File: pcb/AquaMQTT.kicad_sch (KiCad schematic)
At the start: 22 parts, among them J1 DHW MAIN, J2 DHW HMI, J3 LLC 5V, J4 LLC 3V3, J5 Serial, J6 RTC DS3231, J7 Passthrough, Q1 BC547, Q2 BC547, Q3 BC547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

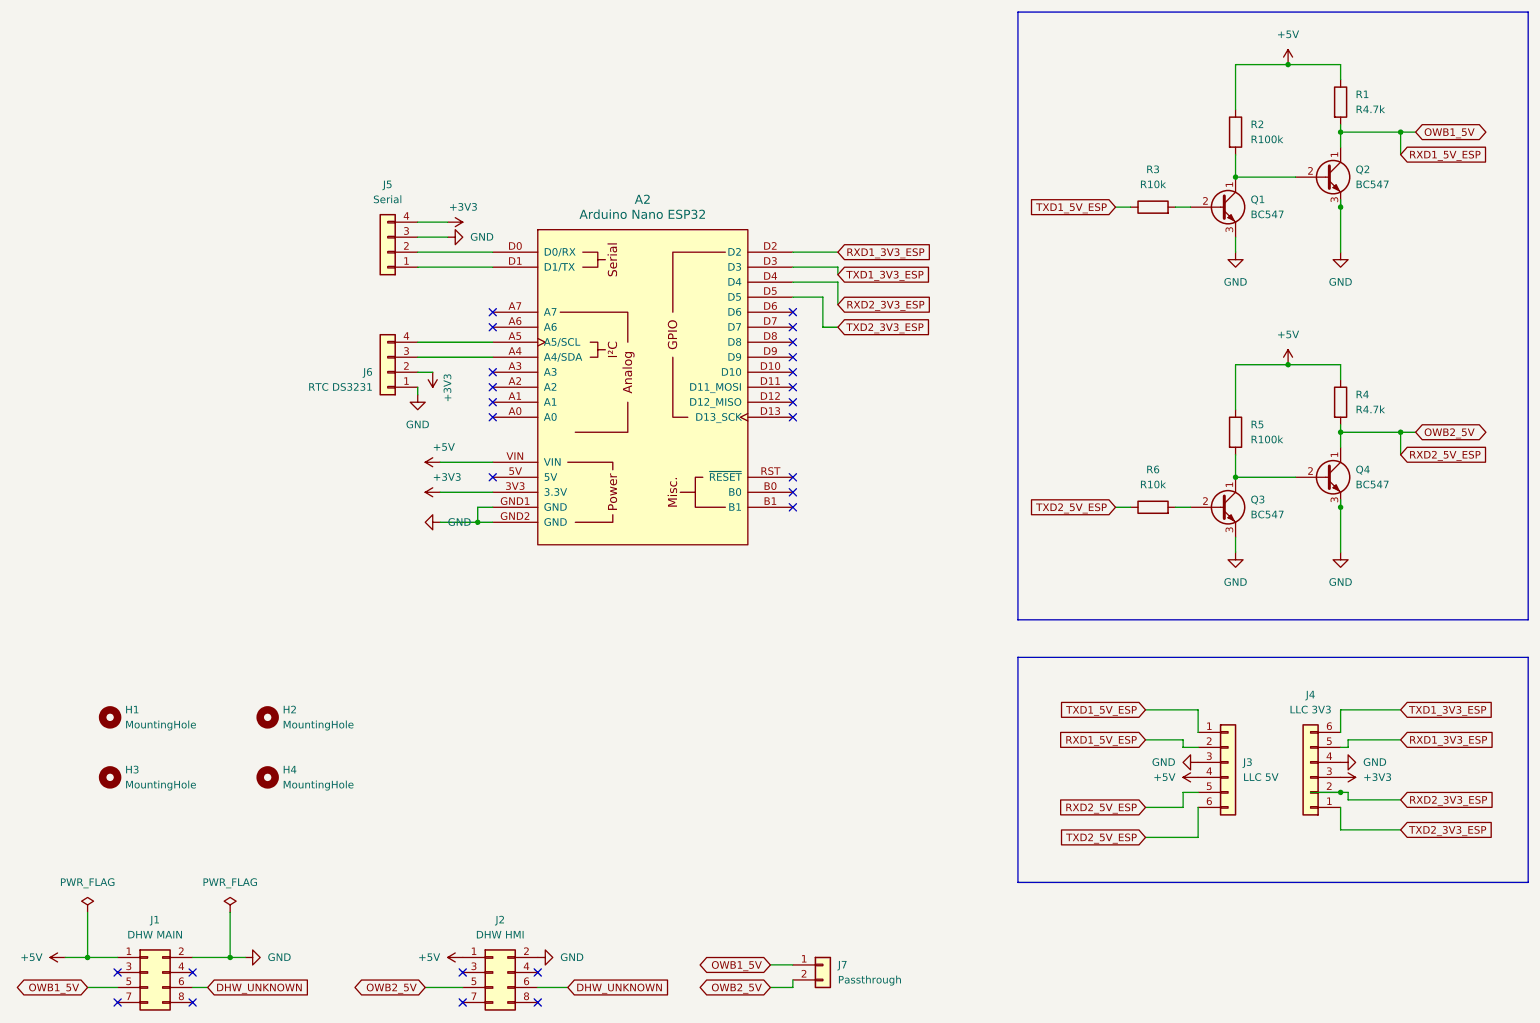
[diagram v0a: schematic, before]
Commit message: feat(pcb): added pcb in rev 2.0 (rast, pre-assembly, sn74lvct45) (#72)
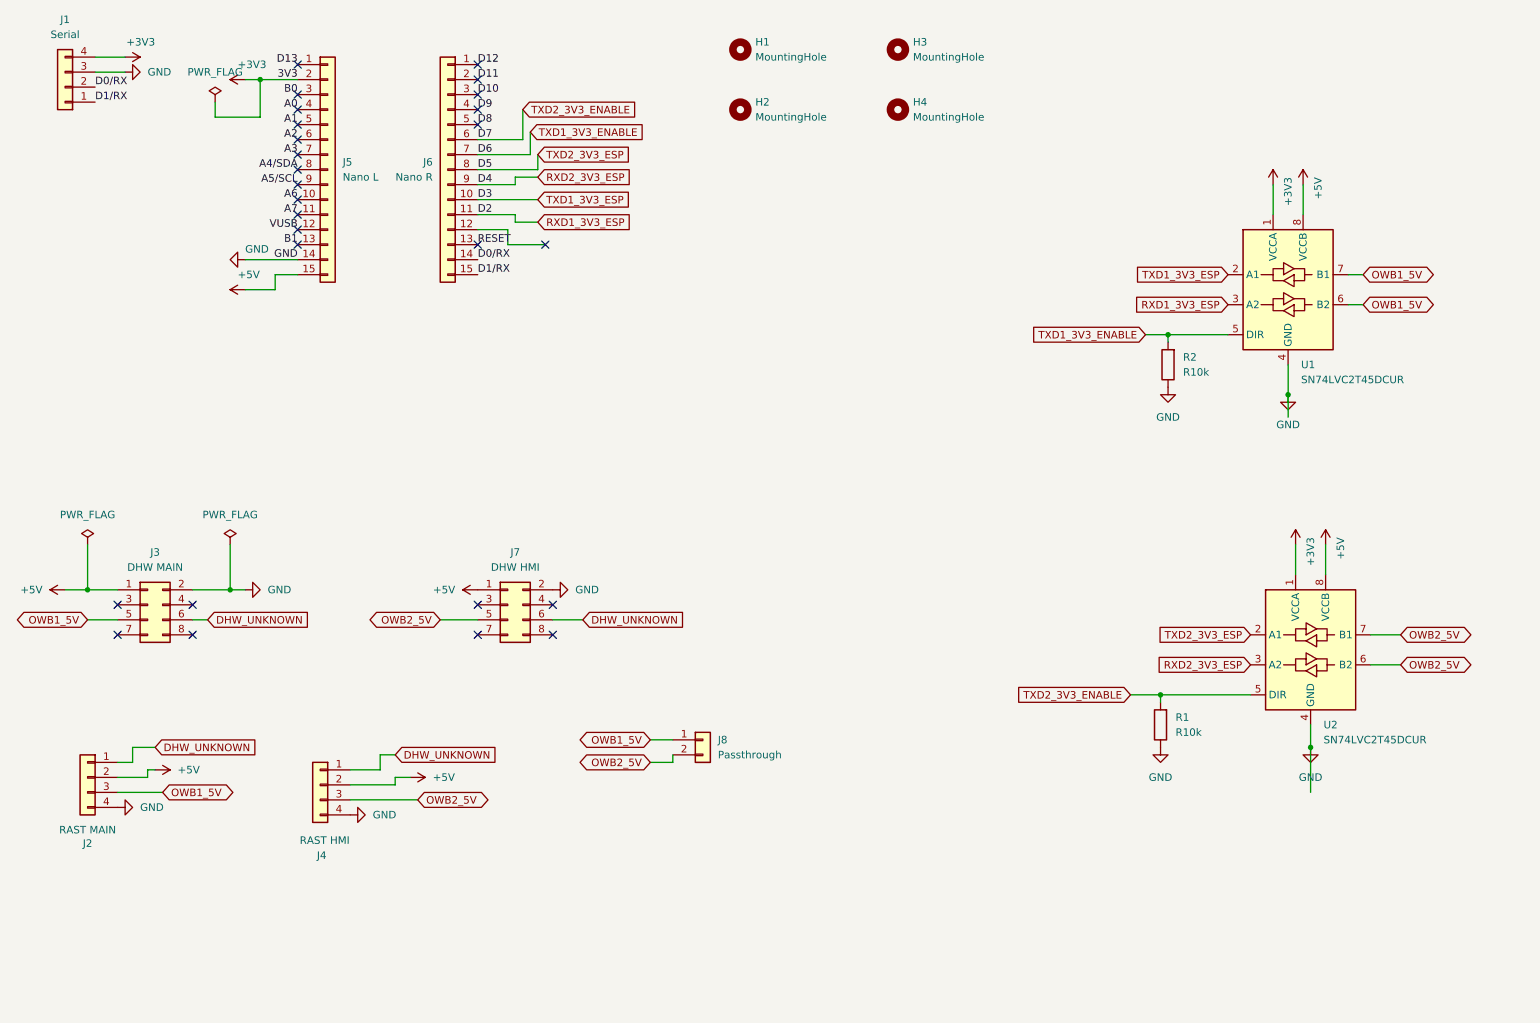
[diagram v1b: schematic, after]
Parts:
- removed A2: Arduino Nano ESP32, PCM_arduino-library:Arduino_Nano_ESP32_Socket, symbol PCM_arduino-library:Arduino_Nano_ESP32_Socket
- removed J3: LLC 5V, Connector_PinSocket_2.54mm:PinSocket_1x06_P2.54mm_Vertical, symbol Connector_Generic:Conn_01x06
- removed J4: LLC 3V3, Connector_PinSocket_2.54mm:PinSocket_1x06_P2.54mm_Vertical, symbol Connector_Generic:Conn_01x06
- removed J6: RTC DS3231, Connector_PinHeader_2.54mm:PinHeader_1x04_P2.54mm_Vertical, symbol Connector_Generic:Conn_01x04
- removed Q1, Q2, Q3, Q4: BC547, Package_TO_SOT_THT:TO-92L_HandSolder, symbol Transistor_BJT:BC547
- removed R2, R5: R100k, Resistor_THT:R_Axial_DIN0411_L9.9mm_D3.6mm_P20.32mm_Horizontal, symbol Device:R
- removed R4: R4.7k, Resistor_THT:R_Axial_DIN0411_L9.9mm_D3.6mm_P20.32mm_Horizontal, symbol Device:R
- removed R6: R10k, Resistor_THT:R_Axial_DIN0411_L9.9mm_D3.6mm_P20.32mm_Horizontal, symbol Device:R
- added J2: RAST MAIN, rast:RAST_3517-06_(2.5MM)_2 COPY, symbol Connector_Generic:Conn_01x04
- added J4: RAST HMI, rast:RAST_3517-06_(2.5MM)_2 COPY, symbol Connector_Generic:Conn_01x04
- added J5: Nano L, Connector_PinSocket_2.54mm:PinSocket_1x15_P2.54mm_Vertical, symbol Connector_Generic:Conn_01x15
- added J6: Nano R, Connector_PinSocket_2.54mm:PinSocket_1x15_P2.54mm_Vertical, symbol Connector_Generic:Conn_01x15
- added U1, U2: SN74LVC2T45DCUR, Package_SO:SSOP-8_2.95x2.8mm_P0.65mm, symbol Logic_LevelTranslator:SN74LVC2T45DCUR
- J1: renamed from J5; footprint Connector_PinSocket_2.54mm:PinSocket_1x04_P2.54mm_Vertical -> Connector_PinHeader_2.54mm:PinHeader_1x04_P2.54mm_Vertical; LCSC (none) -> C5116483
- J3: renamed from J1; LCSC (none) -> C32713277
- J7: renamed from J2; LCSC (none) -> C32713277
- J8: renamed from J7; LCSC (none) -> C5360898
- R1: value R4.7k -> R10k; footprint Resistor_THT:R_Axial_DIN0411_L9.9mm_D3.6mm_P20.32mm_Horizontal -> Resistor_THT:R_Axial_DIN0207_L6.3mm_D2.5mm_P10.16mm_Horizontal; LCSC (none) -> C410695
- R2: renamed from R3; footprint Resistor_THT:R_Axial_DIN0411_L9.9mm_D3.6mm_P20.32mm_Horizontal -> Resistor_THT:R_Axial_DIN0207_L6.3mm_D2.5mm_P10.16mm_Horizontal; LCSC (none) -> C410695
- renumbered H3 to H2, H2 to H3
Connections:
- net TXD1_5V_ESP is gone; now on net GND: R2.1
- net +3V3: now also J5.2 (Pin_2), U1.1 (VCCA), U2.1 (VCCA)
- net +5V: now also J2.2 (Pin_2), J4.2 (Pin_2), J5.15 (Pin_15), U1.8 (VCCB), U2.8 (VCCB); no longer R1.1
- net DHW_UNKNOWN: now also J2.1 (Pin_1), J4.1 (Pin_1)
- net GND: now also R1.1, J2.4 (Pin_4), J4.4 (Pin_4), J5.14 (Pin_14), U1.4 (GND), U2.4 (GND)
- net OWB1_5V: now also J2.3 (Pin_3), U1.6 (B2), U1.7 (B1); no longer R1.2
- net OWB2_5V: now also J4.3 (Pin_3), U2.6 (B2), U2.7 (B1)
- net RXD1_3V3_ESP: now also J6.11 (Pin_11), U1.3 (A2)
- net RXD2_3V3_ESP: now also J6.9 (Pin_9), U2.3 (A2)
- net TXD1_3V3_ESP: now also J6.10 (Pin_10), U1.2 (A1)
- net TXD2_3V3_ESP: now also J6.8 (Pin_8), U2.2 (A1)
- net TXD1_3V3_ENABLE: now reaches R2.2
- net TXD1_3V3_ENABLE: now also J6.7 (Pin_7), U1.5 (DIR)
- net D1/RX: now reaches J1.1 (Pin_1)
- net D1/RX: now also J6.15 (Pin_15)
- net D0/RX: now reaches J1.2 (Pin_2)
- net D0/RX: now also J6.14 (Pin_14)
- new net A0: J5.4 (Pin_4)
- new net A1: J5.5 (Pin_5)
- new net A2: J5.6 (Pin_6)
- new net A3: J5.7 (Pin_7)
- new net A4/SDA: J5.8 (Pin_8)
- new net A5/SCL: J5.9 (Pin_9)
- new net A6: J5.10 (Pin_10)
- new net A7: J5.11 (Pin_11)
- new net B0: J5.3 (Pin_3)
- new net B1: J5.13 (Pin_13)
- new net D10: J6.3 (Pin_3)
- new net D11: J6.2 (Pin_2)
- new net D12: J6.1 (Pin_1)
- new net D13: J5.1 (Pin_1)
- new net D8: J6.5 (Pin_5)
- new net D9: J6.4 (Pin_4)
- new net RESET: J6.13 (Pin_13)
- new net TXD2_3V3_ENABLE: J6.6 (Pin_6), R1.2, U2.5 (DIR)
- new net VUSB: J5.12 (Pin_12)
- no-connect marks 26 -> 27
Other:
- moved on the sheet: H1, H2, H3, H4, J1, J3, J7, J8, R2
